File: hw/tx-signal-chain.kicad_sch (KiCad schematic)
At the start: 21 parts, among them IC1101 NCP164AMT120TAG, IC1102 NCP164AMT120TAG, K1101 G2RL-2, U1101 ICE40UP3K-UWG30ITR1K

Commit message: checkpoint
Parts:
- removed C1101, C1102, C1103: 1uF, symbol Device:C
- removed C1104: 10uF, symbol Device:C
- removed IC1101, IC1102: NCP164AMT120TAG, SON65P200X200X80-7N, symbol NCP164AMT120TAG:NCP164AMT120TAG
- removed R1102: 100k, symbol Device:R_US
- added Q1101: NVMFD5C466NLET1G, NVMFD030N06C, symbol NVMFD5C466NLET1G:NVMFD5C466NLET1G
- added Q1102: 2N7002, Package_TO_SOT_SMD:SOT-23, symbol Transistor_FET:2N7002
- R1101: value 175k -> Rgate=6.8ohms
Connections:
- net VPP_2V5: no longer R1101.1
- net VDD1V2 renamed FPGA1V2
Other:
- note added: "Possible solution for modulation tracking buck converter."
- note removed: "this is WRONG Use STM M0"

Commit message: Making some progress on PIN diode bias boost converter. Page number reorg.
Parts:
- renumbered C1105 to C1101, C1106 to C1102, C1107 to C1103, C1108 to C1104, C1109 to C1105, C1110 to C1106, C1111 to C1107, C1112 to C1108, C1113 to C1109, C1114 to C1110, Q1102 to Q1101, Q1101 to Q1102, R1103 to R1102
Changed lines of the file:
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@@
 		(on_board yes)
 		(dnp no)
-		(property "Reference" "C1110"
+		(property "Reference" "C1106"
 			(at 229.616 149.606 90)
 			(effects
@@
 			(project "USB-SSB-txcvr"
 				(path "/8ae46c04-d01a-4756-8774-512b694bfaff/2406d03c-531b-4eaf-8b4b-4b266b9d0f2b"
-					(reference "C1110")
+					(reference "C1106")
 					(unit 1)
 				)
@@
 		(on_board yes)
 		(dnp no)
-		(property "Reference" "C1108"
+		(property "Reference" "C1104"
 			(at 210.566 149.606 90)
 			(effects
@@
 			(project "USB-SSB-txcvr"
 				(path "/8ae46c04-d01a-4756-8774-512b694bfaff/2406d03c-531b-4eaf-8b4b-4b266b9d0f2b"
-					(reference "C1108")
+					(reference "C1104")
 					(unit 1)
 				)
@@
 		(on_board yes)
 		(dnp no)
-		(property "Reference" "#PWR01110"
+		(property "Reference" "#PWR01102"
 			(at 187.96 166.37 0)
 			(effects
@@
 			(project "USB-SSB-txcvr"
 				(path "/8ae46c04-d01a-4756-8774-512b694bfaff/2406d03c-531b-4eaf-8b4b-4b266b9d0f2b"
-					(reference "#PWR01110")
+					(reference "#PWR01102")
 					(unit 1)
 				)
@@
 		(on_board yes)
 		(dnp no)
-		(property "Reference" "C1109"
+		(property "Reference" "C1105"
 			(at 222.504 149.606 90)
 			(effects
@@
 			(project "USB-SSB-txcvr"
 				(path "/8ae46c04-d01a-4756-8774-512b694bfaff/2406d03c-531b-4eaf-8b4b-4b266b9d0f2b"
-					(reference "C1109")
+					(reference "C1105")
 					(unit 1)
 				)
@@
 		(on_board yes)
 		(dnp no)
-		(property "Reference" "C1113"
+		(property "Reference" "C1109"
 			(at 249.936 117.856 90)
 			(effects
@@
 			(project "USB-SSB-txcvr"
 				(path "/8ae46c04-d01a-4756-8774-512b694bfaff/2406d03c-531b-4eaf-8b4b-4b266b9d0f2b"
-					(reference "C1113")
+					(reference "C1109")
 					(unit 1)
 				)
@@
 		(on_board yes)
 		(dnp no)
-		(property "Reference" "C1111"
+		(property "Reference" "C1107"
 			(at 242.824 117.856 90)
 			(effects
@@
 			(project "USB-SSB-txcvr"
 				(path "/8ae46c04-d01a-4756-8774-512b694bfaff/2406d03c-531b-4eaf-8b4b-4b266b9d0f2b"
-					(reference "C1111")
+					(reference "C1107")
 					(unit 1)
 				)
@@
 		(on_board yes)
 		(dnp no)
-		(property "Reference" "#PWR01117"
+		(property "Reference" "#PWR01111"
 			(at 246.38 165.1 0)
 			(effects
@@
 			(project "USB-SSB-txcvr"
 				(path "/8ae46c04-d01a-4756-8774-512b694bfaff/2406d03c-531b-4eaf-8b4b-4b266b9d0f2b"
-					(reference "#PWR01117")
+					(reference "#PWR01111")
 					(unit 1)
 				)
@@
 		(on_board yes)
 		(dnp no)
-		(property "Reference" "#PWR01116"
+		(property "Reference" "#PWR01109"
 			(at 246.38 134.62 0)
 			(effects
@@
 			(project "USB-SSB-txcvr"
 				(path "/8ae46c04-d01a-4756-8774-512b694bfaff/2406d03c-531b-4eaf-8b4b-4b266b9d0f2b"
-					(reference "#PWR01116")
+					(reference "#PWR01109")
 					(unit 1)
 				)
@@
 		(dnp no)
 		(fields_autoplaced yes)
-		(property "Reference" "#PWR01102"
+		(property "Reference" "#PWR01110"
 			(at 246.38 147.32 0)
 			(effects
@@
 			(project "USB-SSB-txcvr"
 				(path "/8ae46c04-d01a-4756-8774-512b694bfaff/2406d03c-531b-4eaf-8b4b-4b266b9d0f2b"
-					(reference "#PWR01102")
+					(reference "#PWR01110")
 					(unit 1)
 				)
@@
 		(on_board yes)
 		(dnp no)
-		(property "Reference" "C1105"
+		(property "Reference" "C1101"
 			(at 184.404 149.606 90)
 			(effects
@@
 			(project "USB-SSB-txcvr"
 				(path "/8ae46c04-d01a-4756-8774-512b694bfaff/2406d03c-531b-4eaf-8b4b-4b266b9d0f2b"
-					(reference "C1105")
+					(reference "C1101")
 					(unit 1)
 				)
@@
 		(on_board yes)
 		(dnp no)
-		(property "Reference" "C1114"
+		(property "Reference" "C1110"
 			(at 249.936 148.336 90)
 			(effects
@@
 			(project "USB-SSB-txcvr"
 				(path "/8ae46c04-d01a-4756-8774-512b694bfaff/2406d03c-531b-4eaf-8b4b-4b266b9d0f2b"
-					(reference "C1114")
+					(reference "C1110")
 					(unit 1)
 				)
@@
 		(dnp no)
 		(fields_autoplaced yes)
-		(property "Reference" "Q1102"
+		(property "Reference" "Q1101"
 			(at 46.99 126.9999 0)
 			(effects
@@
 			(project ""
 				(path "/8ae46c04-d01a-4756-8774-512b694bfaff/2406d03c-531b-4eaf-8b4b-4b266b9d0f2b"
-					(reference "Q1102")
+					(reference "Q1101")
 					(unit 1)
 				)
@@
 		(on_board yes)
 		(dnp no)
-		(property "Reference" "C1112"
+		(property "Reference" "C1108"
 			(at 242.824 148.336 90)
 			(effects
@@
 			(project "USB-SSB-txcvr"
 				(path "/8ae46c04-d01a-4756-8774-512b694bfaff/2406d03c-531b-4eaf-8b4b-4b266b9d0f2b"
-					(reference "C1112")
+					(reference "C1108")
 					(unit 1)
 				)
@@
 		(on_board yes)
 		(dnp no)
-		(property "Reference" "C1106"
+		(property "Reference" "C1102"
 			(at 191.516 149.606 90)
 			(effects
@@
 			(project "USB-SSB-txcvr"
 				(path "/8ae46c04-d01a-4756-8774-512b694bfaff/2406d03c-531b-4eaf-8b4b-4b266b9d0f2b"
-					(reference "C1106")
+					(reference "C1102")
 					(unit 1)
 				)
@@
 		(dnp no)
 		(fields_autoplaced yes)
-		(property "Reference" "Q1101"
+		(property "Reference" "Q1102"
 			(at 131.318 115.316 0)
 			(effects
@@
 			(project ""
 				(path "/8ae46c04-d01a-4756-8774-512b694bfaff/2406d03c-531b-4eaf-8b4b-4b266b9d0f2b"
-					(reference "Q1101")
+					(reference "Q1102")
 					(unit 1)
 				)
@@
 		(dnp no)
 		(fields_autoplaced yes)
-		(property "Reference" "#PWR01101"
+		(property "Reference" "#PWR01108"
 			(at 246.38 107.95 0)
 			(effects
@@
 			(project ""
 				(path "/8ae46c04-d01a-4756-8774-512b694bfaff/2406d03c-531b-4eaf-8b4b-4b266b9d0f2b"
-					(reference "#PWR01101")
+					(reference "#PWR01108")
 					(unit 1)
 				)
@@
 		(dnp no)
 		(fields_autoplaced yes)
-		(property "Reference" "R1103"
+		(property "Reference" "R1102"
 			(at 248.92 107.9499 0)
 			(effects
@@
 			(project ""
 				(path "/8ae46c04-d01a-4756-8774-512b694bfaff/2406d03c-531b-4eaf-8b4b-4b266b9d0f2b"
-					(reference "R1103")
+					(reference "R1102")
 					(unit 1)
 				)
@@
 		(dnp no)
 		(fields_autoplaced yes)
-		(property "Reference" "#PWR01114"
+		(property "Reference" "#PWR01106"
 			(at 226.06 148.59 0)
 			(effects
@@
 			(project "USB-SSB-txcvr"
 				(path "/8ae46c04-d01a-4756-8774-512b694bfaff/2406d03c-531b-4eaf-8b4b-4b266b9d0f2b"
-					(reference "#PWR01114")
+					(reference "#PWR01106")
 					(unit 1)
 				)
@@
 		(dnp no)
 		(fields_autoplaced yes)
-		(property "Reference" "#PWR01109"
+		(property "Reference" "#PWR01101"
 			(at 187.96 148.59 0)
 			(effects
@@
 			(project "USB-SSB-txcvr"
 				(path "/8ae46c04-d01a-4756-8774-512b694bfaff/2406d03c-531b-4eaf-8b4b-4b266b9d0f2b"
-					(reference "#PWR01109")
+					(reference "#PWR01101")
 					(unit 1)
 				)
@@
 		(on_board yes)
 		(dnp no)
-		(property "Reference" "C1107"
+		(property "Reference" "C1103"
 			(at 203.454 149.606 90)
 			(effects
@@
 			(project "USB-SSB-txcvr"
 				(path "/8ae46c04-d01a-4756-8774-512b694bfaff/2406d03c-531b-4eaf-8b4b-4b266b9d0f2b"
-					(reference "C1107")
+					(reference "C1103")
 					(unit 1)
 				)
@@
 		(on_board yes)
 		(dnp no)
-		(property "Reference" "#PWR01115"
+		(property "Reference" "#PWR01107"
 			(at 226.06 166.37 0)
 			(effects
@@
 			(project "USB-SSB-txcvr"
 				(path "/8ae46c04-d01a-4756-8774-512b694bfaff/2406d03c-531b-4eaf-8b4b-4b266b9d0f2b"
-					(reference "#PWR01115")
+					(reference "#PWR01107")
 					(unit 1)
 				)
@@
 		(on_board yes)
 		(dnp no)
-		(property "Reference" "#PWR01113"
+		(property "Reference" "#PWR01105"
 			(at 208.28 123.19 0)
 			(effects
@@
 			(project "USB-SSB-txcvr"
 				(path "/8ae46c04-d01a-4756-8774-512b694bfaff/2406d03c-531b-4eaf-8b4b-4b266b9d0f2b"
-					(reference "#PWR01113")
+					(reference "#PWR01105")
 					(unit 1)
 				)
@@
 		(on_board yes)
 		(dnp no)
-		(property "Reference" "#PWR01112"
+		(property "Reference" "#PWR01104"
 			(at 207.01 166.37 0)
 			(effects
@@
 			(project "USB-SSB-txcvr"
 				(path "/8ae46c04-d01a-4756-8774-512b694bfaff/2406d03c-531b-4eaf-8b4b-4b266b9d0f2b"
-					(reference "#PWR01112")
+					(reference "#PWR01104")
 					(unit 1)
 				)
@@
 		(dnp no)
 		(fields_autoplaced yes)
-		(property "Reference" "#PWR01111"
+		(property "Reference" "#PWR01103"
 			(at 207.01 148.59 0)
 			(effects
@@
 			(project "USB-SSB-txcvr"
 				(path "/8ae46c04-d01a-4756-8774-512b694bfaff/2406d03c-531b-4eaf-8b4b-4b266b9d0f2b"
-					(reference "#PWR01111")
-					(unit 1)
-				)
+					(reference "#PWR01103")
+					(unit 1)
+				)

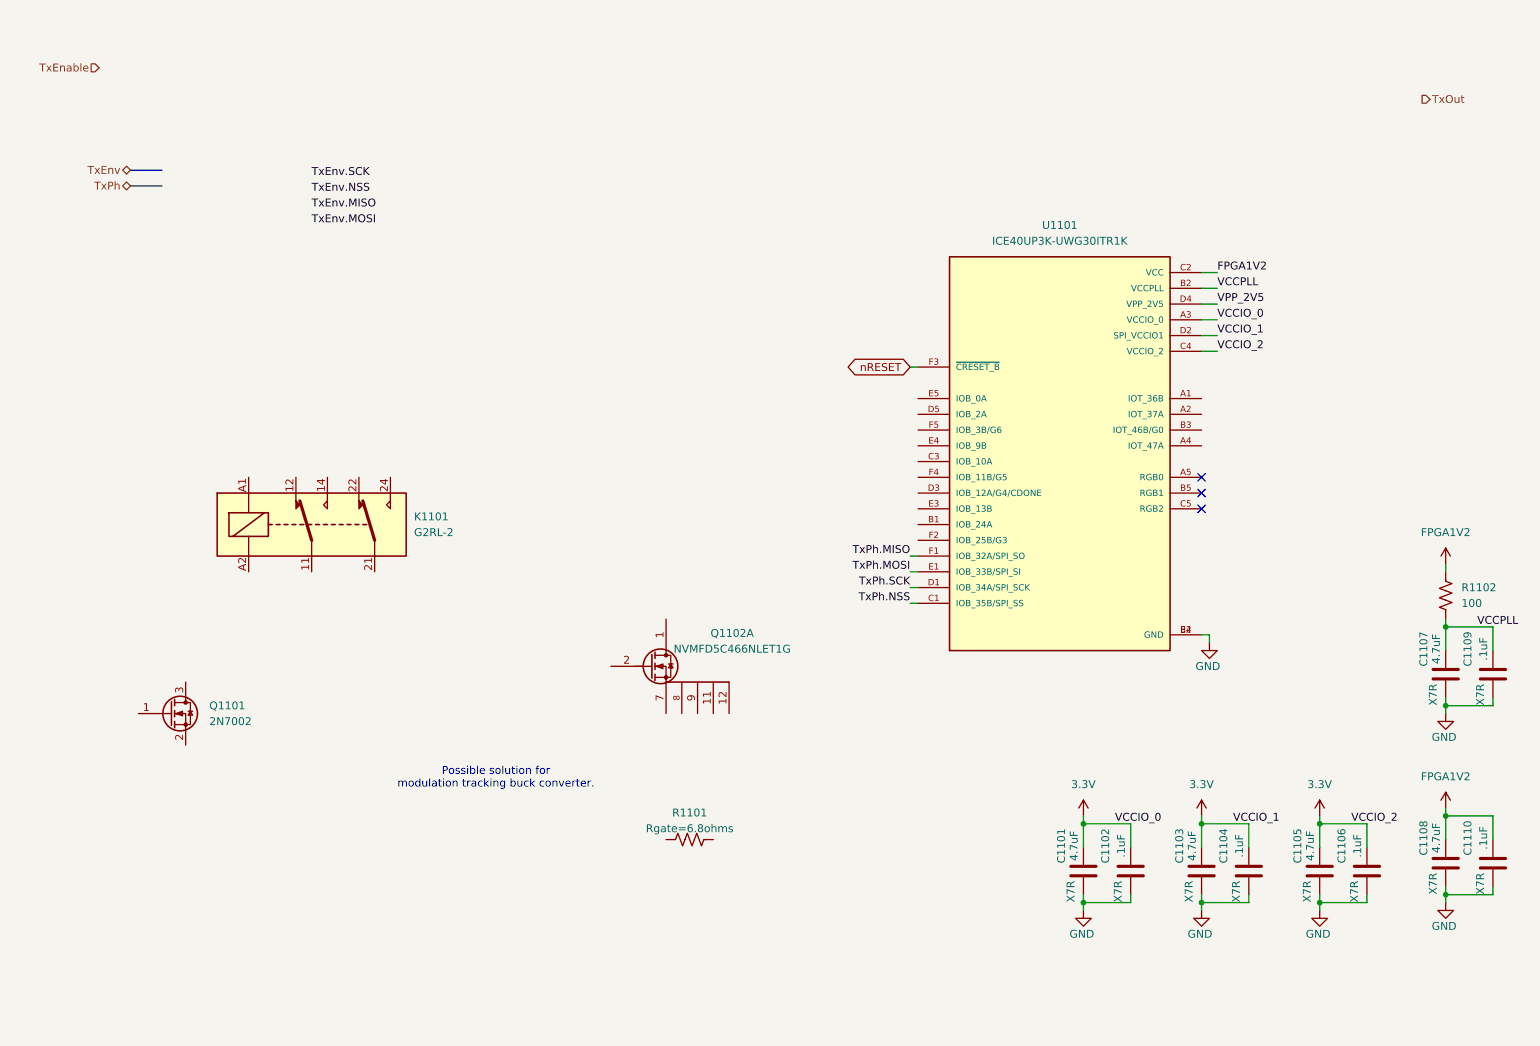
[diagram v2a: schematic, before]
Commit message: Starting to dev the LC tanks for the power MOSFET output stage.
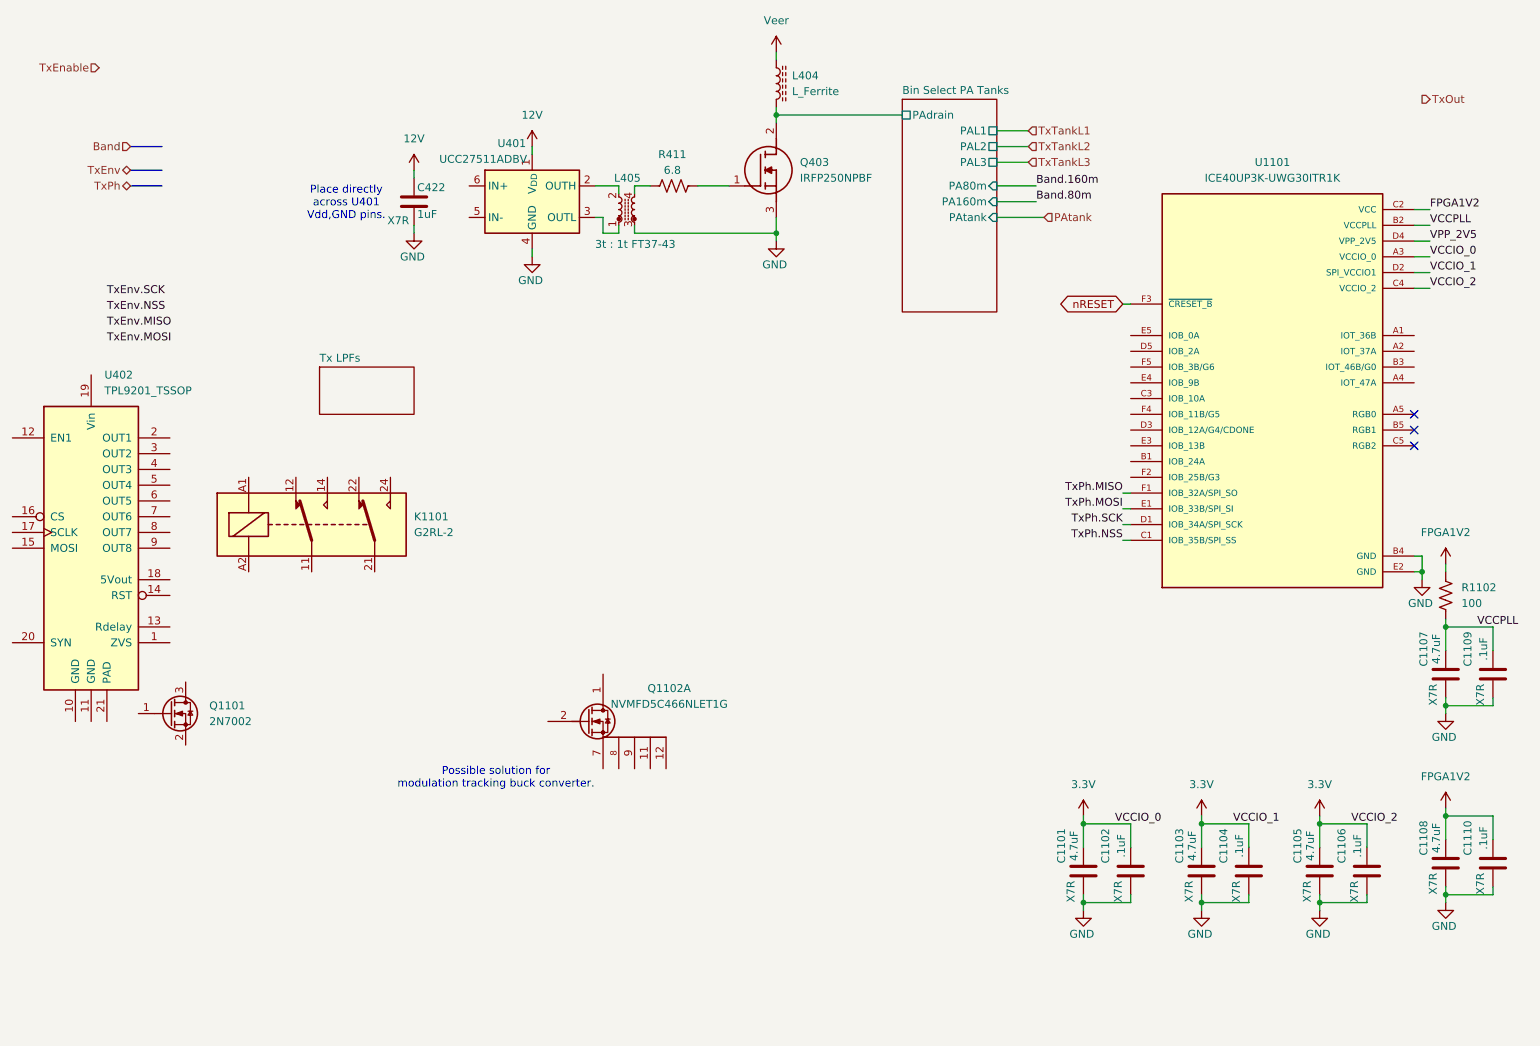
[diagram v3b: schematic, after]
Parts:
- removed R1101: Rgate=6.8ohms, symbol Device:R_US
- added C422: 1uF, symbol Device:C
- added L404: L_Ferrite, symbol Device:L_Ferrite
- added L405: 3t : 1t FT37-43, symbol Device:L_Ferrite_Coupled_Small
- added Q403: IRFP250NPBF, TO545P530X1560X2460-3P, symbol IRFP250NPBF:IRFP250NPBF
- added R411: 6.8, symbol Device:R_US
- added U401: UCC27511ADBV, Package_TO_SOT_SMD:SOT-23-6, symbol Driver_FET:UCC27511ADBV
- added U402: TPL9201_TSSOP, Package_SO:HTSSOP-20-1EP_4.4x6.5mm_P0.65mm_EP3.4x6.5mm_ThermalVias, symbol Driver_Relay:TPL9201_TSSOP
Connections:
- net GND: now also C422.2, L405.3, Q403.3 (S), U401.4 (GND)
- new net: L405.2, U401.2 (OUTH)
- new net: L405.1, U401.3 (OUTL)
- new net: L405.4, R411.1
- new net: Q403.1 (G), R411.2
- new net 12V: C422.1, U401.1 (V_{DD})
- new net Bin Select PA Tanks/PAdrain: L404.2, Q403.2 (D)
- new net Veer: L404.1
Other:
- added sheet Bin Select PA Tanks (pa-tanks.kicad_sch)
- added sheet Tx LPFs (tx-LPFs.kicad_sch)
- note added: "Place directly across U401 Vdd,GND pins."
- moved on the sheet: Q1102A

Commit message: Getting closer to having the PA LC tank switching done
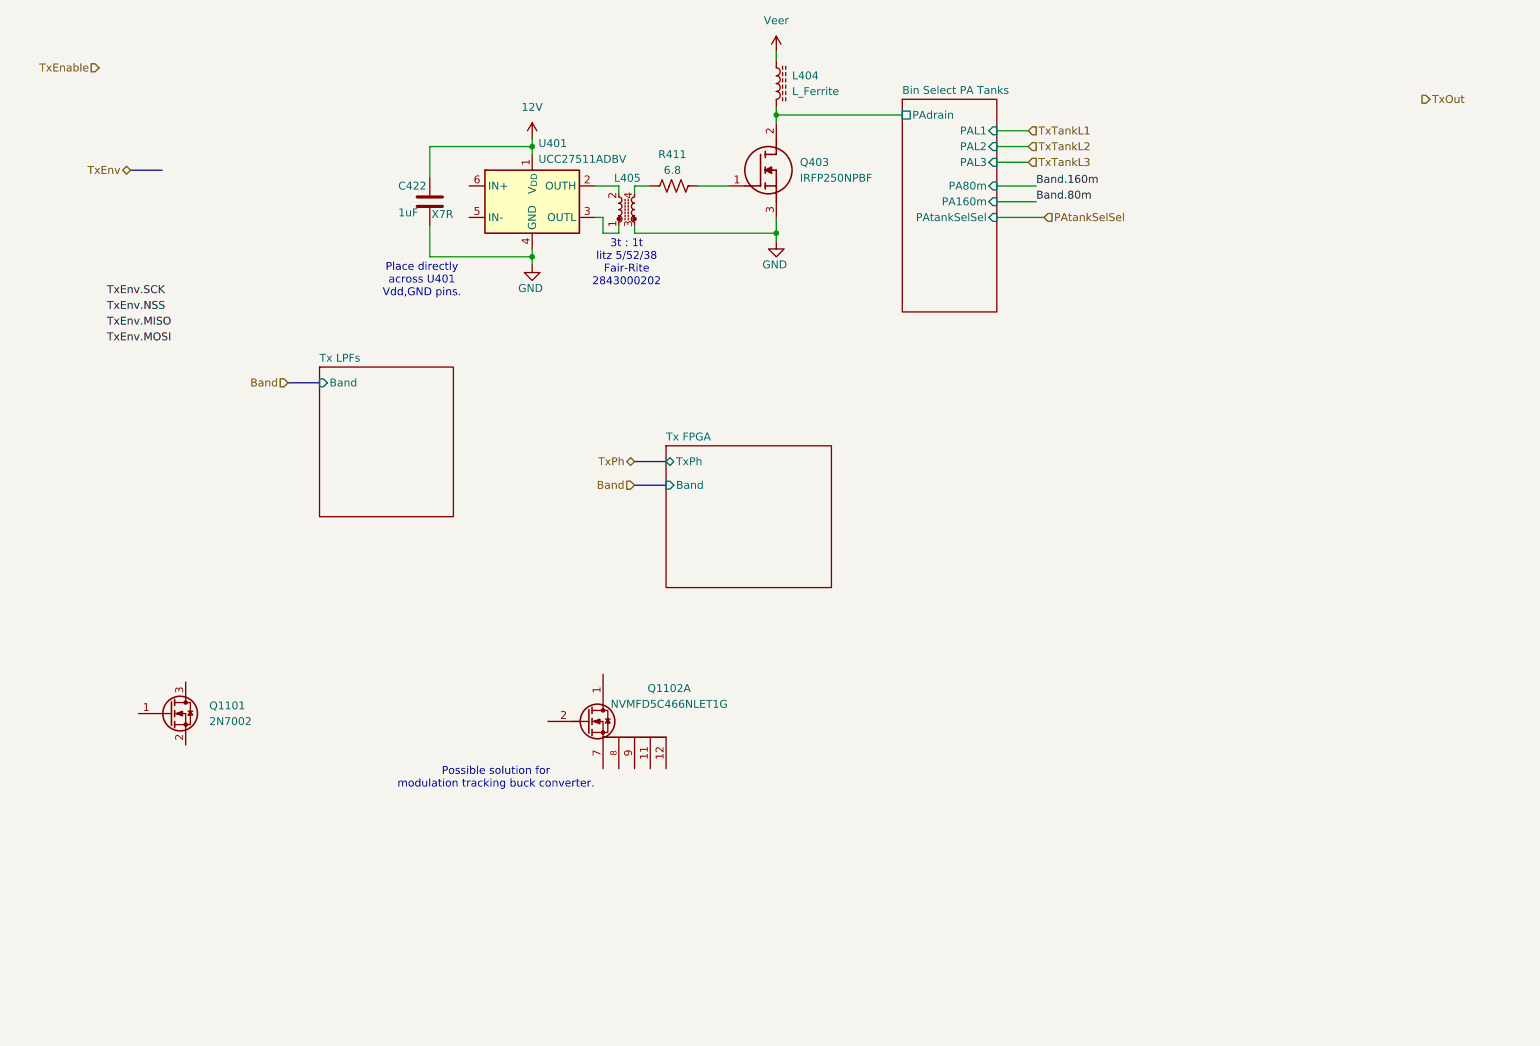
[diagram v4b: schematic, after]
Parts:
- removed C1101, C1103, C1105, C1107, C1108: 4.7uF, symbol Device:C
- removed C1102, C1104, C1106, C1109, C1110: .1uF, symbol Device:C
- removed K1101: G2RL-2, Relay_THT:Relay_DPDT_Omron_G2RL-2, symbol Relay:G2RL-2
- removed R1102: 100, symbol Device:R_US
- removed U1101: ICE40UP3K-UWG30ITR1K, ICE40UP3K-UWG30ITR1K:BGA30N40P6X5_253X211X60N, symbol ICE40UP3K-UWG30ITR1K:ICE40UP3K-UWG30ITR1K
- removed U402: TPL9201_TSSOP, Package_SO:HTSSOP-20-1EP_4.4x6.5mm_P0.65mm_EP3.4x6.5mm_ThermalVias, symbol Driver_Relay:TPL9201_TSSOP
- L405: value 3t : 1t FT37-43 -> ~
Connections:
- no-connect marks 3 -> 0
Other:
- added sheet Tx FPGA (tx-fpga.kicad_sch)
- sheet Bin Select PA Tanks ports: added PAtankSelSel; removed PAtank
- sheet Tx LPFs ports: added Band; removed none
- note added: "3t : 1t litz 5/52/38 Fair-Rite 2843000202"
- moved on the sheet: C422
